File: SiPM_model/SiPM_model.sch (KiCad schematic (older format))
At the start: 11 parts

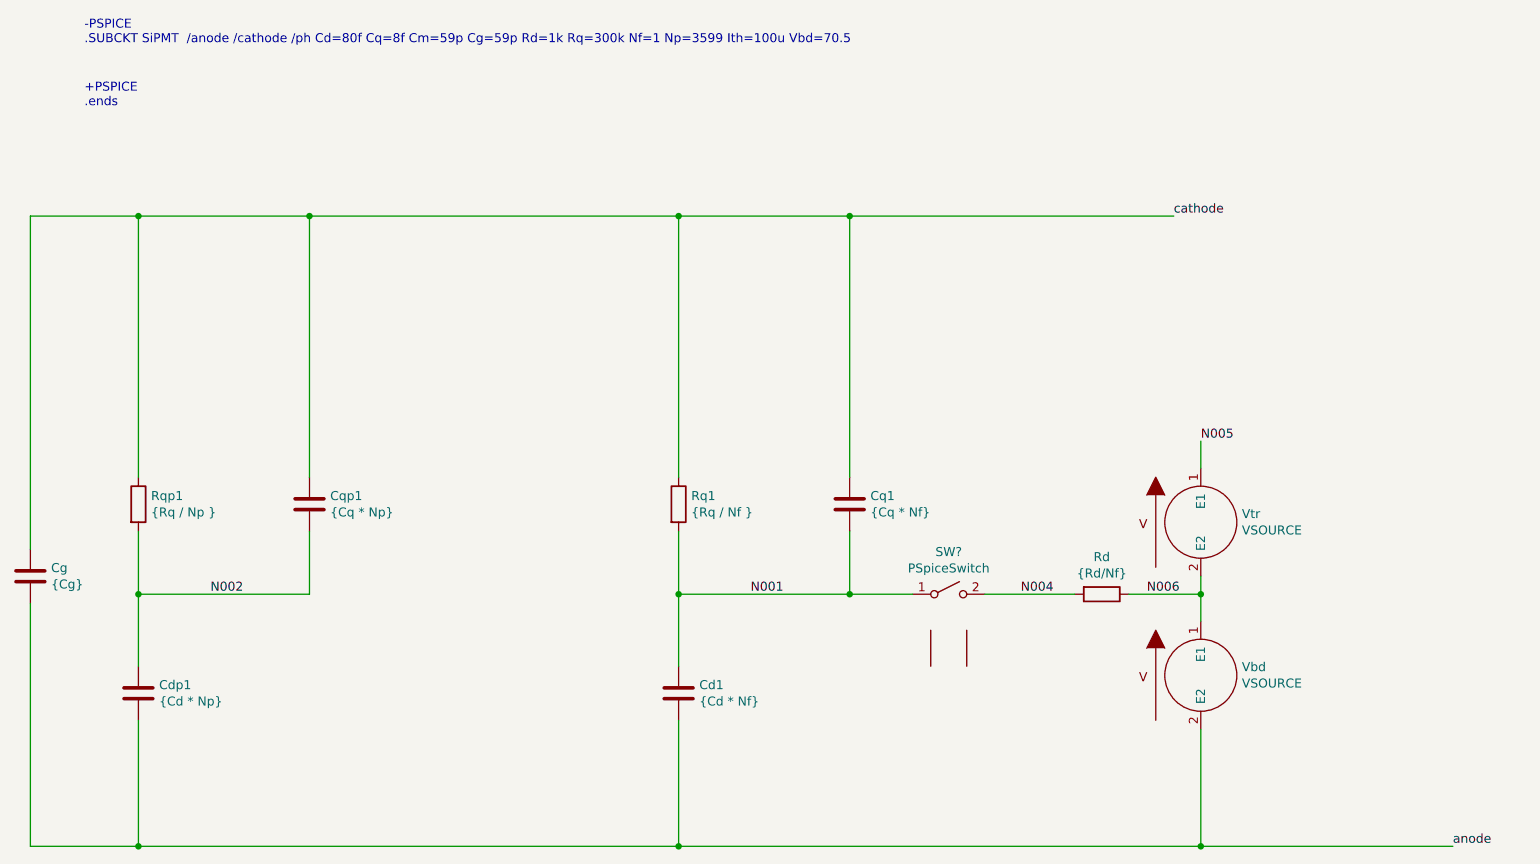
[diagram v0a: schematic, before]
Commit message: Adding SiPM model as KiCAD schematic
Added more information to README
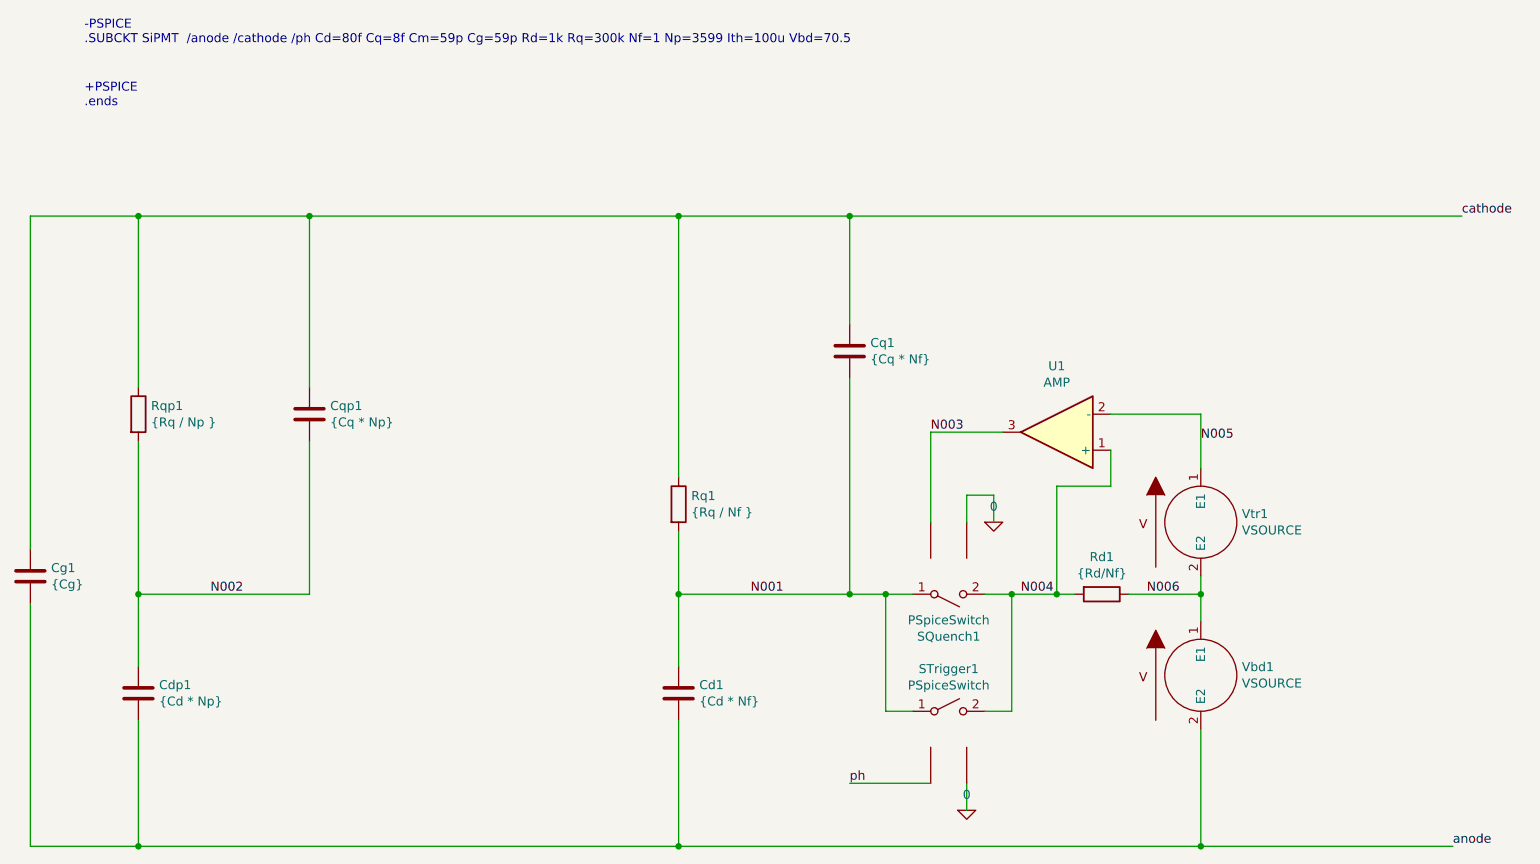
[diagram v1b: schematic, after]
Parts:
- added STrigger1: PSpiceSwitch, symbol PSpiceSwitch:PSpiceSwitch
- added U1: AMP, symbol amp:AMP
- gave numbers to parts that had none: 1
- renumbered Cg to Cg1, Rd to Rd1, Vbd to Vbd1, Vtr to Vtr1
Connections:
- net N001: now also STrigger1.1 (A)
- net N004: now also STrigger1.2 (B), U1.1 (+)
- net N005: now also U1.2 (-)
- net N003: now reaches SQuench1.~ (IN-)
- net N003: now also U1.3
- new net 0: SQuench1.~ (IN-), STrigger1.~ (IN-)
- new net ph: STrigger1.~ (IN-)
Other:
- moved on the sheet: Cq1, Cqp1, Rqp1, SQuench1
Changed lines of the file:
@@
 EESchema Schematic File Version 4
+LIBS:SiPM_model-cache
 EELAYER 26 0
 EELAYER END
@@
 L Device:R Rqp1
 U 1 1 5C4192FE
-P 1750 4100
-F 0 "Rqp1" H 1820 4146 50  0000 L CNN
-F 1 "{Rq / Np }" H 1820 4055 50  0000 L CNN
-F 2 "" V 1680 4100 50  0001 C CNN
-F 3 "~" H 1750 4100 50  0001 C CNN
-	1    1750 4100
+P 1750 3600
+F 0 "Rqp1" H 1820 3646 50  0000 L CNN
+F 1 "{Rq / Np }" H 1820 3555 50  0000 L CNN
+F 2 "" V 1680 3600 50  0001 C CNN
+F 3 "~" H 1750 3600 50  0001 C CNN
+	1    1750 3600
 	1    0    0    -1
 $EndComp
@@
 L Device:C Cqp1
 U 1 1 5C4193BF
-P 2700 4100
-F 0 "Cqp1" H 2815 4146 50  0000 L CNN
-F 1 "{Cq * Np}" H 2815 4055 50  0000 L CNN
-F 2 "" H 2738 3950 50  0001 C CNN
-F 3 "~" H 2700 4100 50  0001 C CNN
-	1    2700 4100
+P 2700 3600
+F 0 "Cqp1" H 2815 3646 50  0000 L CNN
+F 1 "{Cq * Np}" H 2815 3555 50  0000 L CNN
+F 2 "" H 2738 3450 50  0001 C CNN
+F 3 "~" H 2700 3600 50  0001 C CNN
+	1    2700 3600
 	1    0    0    -1
 $EndComp
@@
 $EndComp
 Wire Wire Line
-	1750 3950 1750 2500
+	1750 3450 1750 2500
 Wire Wire Line
 	1750 2500 2700 2500
 Wire Wire Line
-	1750 4250 1750 4600
-Wire Wire Line
-	2700 4250 2700 4600
+	1750 3750 1750 4600
+Wire Wire Line
+	2700 3750 2700 4600
 Wire Wire Line
 	2700 4600 1750 4600
@@
 	1750 6000 4750 6000
 Wire Wire Line
-	2700 3950 2700 2500
+	2700 3450 2700 2500
 Connection ~ 2700 2500
 Wire Wire Line
 	2700 2500 4750 2500
-Text Label 7500 2500 0    50   ~ 0
+Text Label 9100 2500 0    50   ~ 0
 cathode
 Text Label 9050 6000 0    50   ~ 0
@@
 L Device:C Cq1
 U 1 1 5C41A804
-P 5700 4100
-F 0 "Cq1" H 5815 4146 50  0000 L CNN
-F 1 "{Cq * Nf}" H 5815 4055 50  0000 L CNN
-F 2 "" H 5738 3950 50  0001 C CNN
-F 3 "~" H 5700 4100 50  0001 C CNN
-	1    5700 4100
+P 5700 3250
+F 0 "Cq1" H 5815 3296 50  0000 L CNN
+F 1 "{Cq * Nf}" H 5815 3205 50  0000 L CNN
+F 2 "" H 5738 3100 50  0001 C CNN
+F 3 "~" H 5700 3250 50  0001 C CNN
+	1    5700 3250
 	1    0    0    -1
 $EndComp
@@
 	4750 4250 4750 4600
 Wire Wire Line
-	5700 4250 5700 4600
+	5700 3400 5700 4600
 Wire Wire Line
 	5700 4600 4750 4600
@@
 	4750 5300 4750 6000
 Wire Wire Line
-	5700 3950 5700 2500
+	5700 3100 5700 2500
 Text Label 5150 4600 0    50   ~ 0
 N001
@@
 Connection ~ 5700 2500
 Wire Wire Line
-	5700 2500 7500 2500
-$Comp
-L pspice:VSOURCE Vbd
+	5700 2500 9100 2500
+$Comp
+L pspice:VSOURCE Vbd1
 U 1 1 5C41B2E0
 P 7650 5050
-F 0 "Vbd" H 7878 5096 50  0000 L CNN
+F 0 "Vbd1" H 7878 5096 50  0000 L CNN
 F 1 "VSOURCE" H 7878 5005 50  0000 L CNN
 F 2 "" H 7650 5050 50  0001 C CNN
@@
 $EndComp
 $Comp
-L pspice:VSOURCE Vtr
+L pspice:VSOURCE Vtr1
 U 1 1 5C41B4C0
 P 7650 4200
-F 0 "Vtr" H 7878 4246 50  0000 L CNN
+F 0 "Vtr1" H 7878 4246 50  0000 L CNN
 F 1 "VSOURCE" H 7878 4155 50  0000 L CNN
 F 2 "" H 7650 4200 50  0001 C CNN
@@
 Wire Wire Line
 	7650 6000 9050 6000
-Wire Wire Line
-	7650 3900 7650 3750
 Text Label 7350 4600 0    50   ~ 0
 N006
@@
 N005
 $Comp
-L Device:R Rd
+L Device:R Rd1
 U 1 1 5C420582
 P 7100 4600
-F 0 "Rd" V 6893 4600 50  0000 C CNN
+F 0 "Rd1" V 6893 4600 50  0000 C CNN
 F 1 "{Rd/Nf}" V 6984 4600 50  0000 C CNN
 F 2 "" V 7030 4600 50  0001 C CNN
@@
 Wire Wire Line
 	7650 4600 7250 4600
-Wire Wire Line
-	6450 4600 6950 4600
 Text Label 6650 4600 0    50   ~ 0
 N004
 $Comp
-L Device:C Cg
+L Device:C Cg1
 U 1 1 5C4217B8
 P 1150 4500
-F 0 "Cg" H 1265 4546 50  0000 L CNN
+F 0 "Cg1" H 1265 4546 50  0000 L CNN
 F 1 "{Cg}" H 1265 4455 50  0000 L CNN
 F 2 "" H 1188 4350 50  0001 C CNN
@@
 Connection ~ 1750 6000
 $Comp
-L PSpiceSwitch:PSpiceSwitch SW?
+L PSpiceSwitch:PSpiceSwitch SQuench1
 U 1 1 5C4265C3
 P 6250 4600
-F 0 "SW?" H 6250 4835 50  0000 C CNN
+F 0 "SQuench1" H 6250 4835 50  0000 C CNN
 F 1 "PSpiceSwitch" H 6250 4744 50  0000 C CNN
 F 2 "" H 6250 4600 50  0001 C CNN
 F 3 "" H 6250 4600 50  0001 C CNN
 	1    6250 4600
-	1    0    0    -1
-$EndComp
-Wire Wire Line
-	6050 4600 5700 4600
+	1    0    0    1
+$EndComp
+Wire Wire Line
+	6050 4600 5900 4600
 Connection ~ 5700 4600
 Wire Wire Line
@@
 Wire Wire Line
 	7650 4600 7650 4750
+$Comp
+L amp:AMP U1
+U 1 1 5C46E9DF
+P 6850 3700
+F 0 "U1" H 6850 3333 50  0000 C CNN
+F 1 "AMP" H 6850 3424 50  0000 C CNN
+F 2 "" H 6850 3700 50  0001 C CNN
+F 3 "" H 6850 3700 50  0001 C CNN
+	1    6850 3700
+	-1   0    0    1
+$EndComp
+$Comp
+L pspice:0 #GND02
+U 1 1 5C46EB40
+P 6500 4200
+F 0 "#GND02" H 6500 4100 50  0001 C CNN
+F 1 "0" H 6500 4287 50  0000 C CNN
+F 2 "" H 6500 4200 50  0001 C CNN
+F 3 "~" H 6500 4200 50  0001 C CNN
+	1    6500 4200
+	1    0    0    -1
+$EndComp
+Wire Wire Line
+	6500 4200 6500 4050
+Wire Wire Line
+	6500 4050 6350 4050
+Wire Wire Line
+	6350 4050 6350 4200
+Wire Wire Line
+	6550 3700 6150 3700
+Wire Wire Line
+	6150 3700 6150 4200
+Wire Wire Line
+	6850 4600 6850 4000
+Wire Wire Line
+	6850 4000 7150 4000
+Wire Wire Line
+	7150 4000 7150 3800
+Connection ~ 6850 4600
+Wire Wire Line
+	6850 4600 6950 4600
+Wire Wire Line
+	7150 3600 7650 3600
+Wire Wire Line
+	7650 3600 7650 3900
+$Comp
+L PSpiceSwitch:PSpiceSwitch STrigger1
+U 1 1 5C47010D
+P 6250 5250
+F 0 "STrigger1" H 6250 5485 50  0000 C CNN
+F 1 "PSpiceSwitch" H 6250 5394 50  0000 C CNN
+F 2 "" H 6250 5250 50  0001 C CNN
+F 3 "" H 6250 5250 50  0001 C CNN
+	1    6250 5250
+	1    0    0    -1
+$EndComp
+$Comp
+L pspice:0 #GND01
+U 1 1 5C470828
+P 6350 5800
+F 0 "#GND01" H 6350 5700 50  0001 C CNN
+F 1 "0" H 6350 5887 50  0000 C CNN
+F 2 "" H 6350 5800 50  0001 C CNN
+F 3 "~" H 6350 5800 50  0001 C CNN
+	1    6350 5800
+	1    0    0    -1
+$EndComp
+Wire Wire Line
+	6350 5800 6350 5650
+Wire Wire Line
+	5700 5650 6150 5650
+Text Label 5700 5650 0    50   ~ 0
+ph
+Wire Wire Line
+	6450 5250 6600 5250
+Wire Wire Line
+	6600 5250 6600 4600
+Wire Wire Line
+	6450 4600 6600 4600
+Connection ~ 6600 4600
+Wire Wire Line
+	6600 4600 6850 4600
+Wire Wire Line
+	6050 5250 5900 5250
+Wire Wire Line
+	5900 5250 5900 4600
+Connection ~ 5900 4600
+Wire Wire Line
+	5900 4600 5700 4600
+Text Label 6150 3700 0    50   ~ 0
+N003
 $EndSCHEMATC
